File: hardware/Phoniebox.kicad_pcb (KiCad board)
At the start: 2 copper layers, 65 x 56.5 mm, 84 parts, among them J1 GPIO, J2 Screw_Terminal_01x08, J3 Screw_Terminal_01x08, J4 Screw_Terminal_01x08, J5 Conn_02x02_Odd_Even, J7 USB_C_Receptacle_USB2.0, J8 Conn_02x04_Odd_Even, Q1 2N7002, Q2 2N7002, Q3 2N7002, Q4 2N7002, Q5 2N7002, Q6 2N7002, Q7 AO3401A, Q8 2N7002, U1 PAM8406, U2 TPS79333-EP, U3 PCM5102, U4 CAT24C32

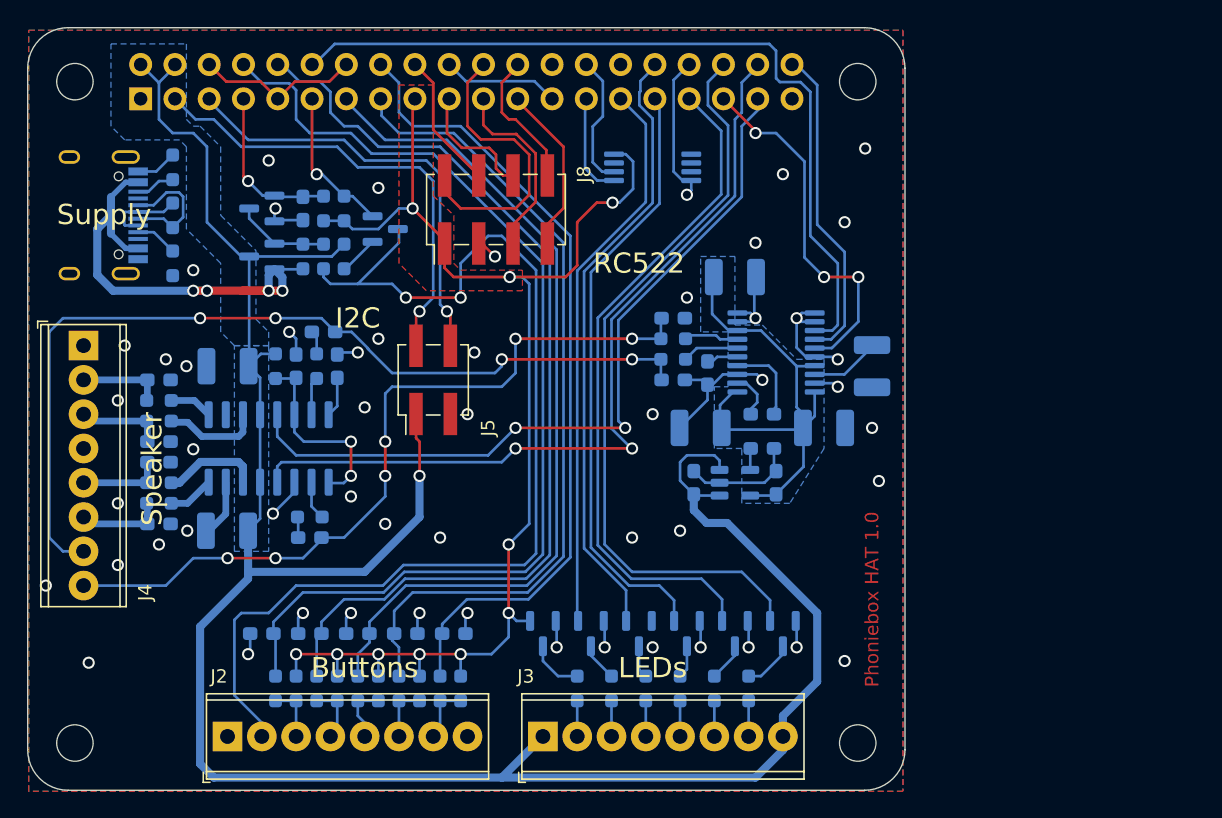
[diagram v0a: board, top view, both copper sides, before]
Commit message: Smaller high value caps. Standard R/C footprints instead of hand solder.
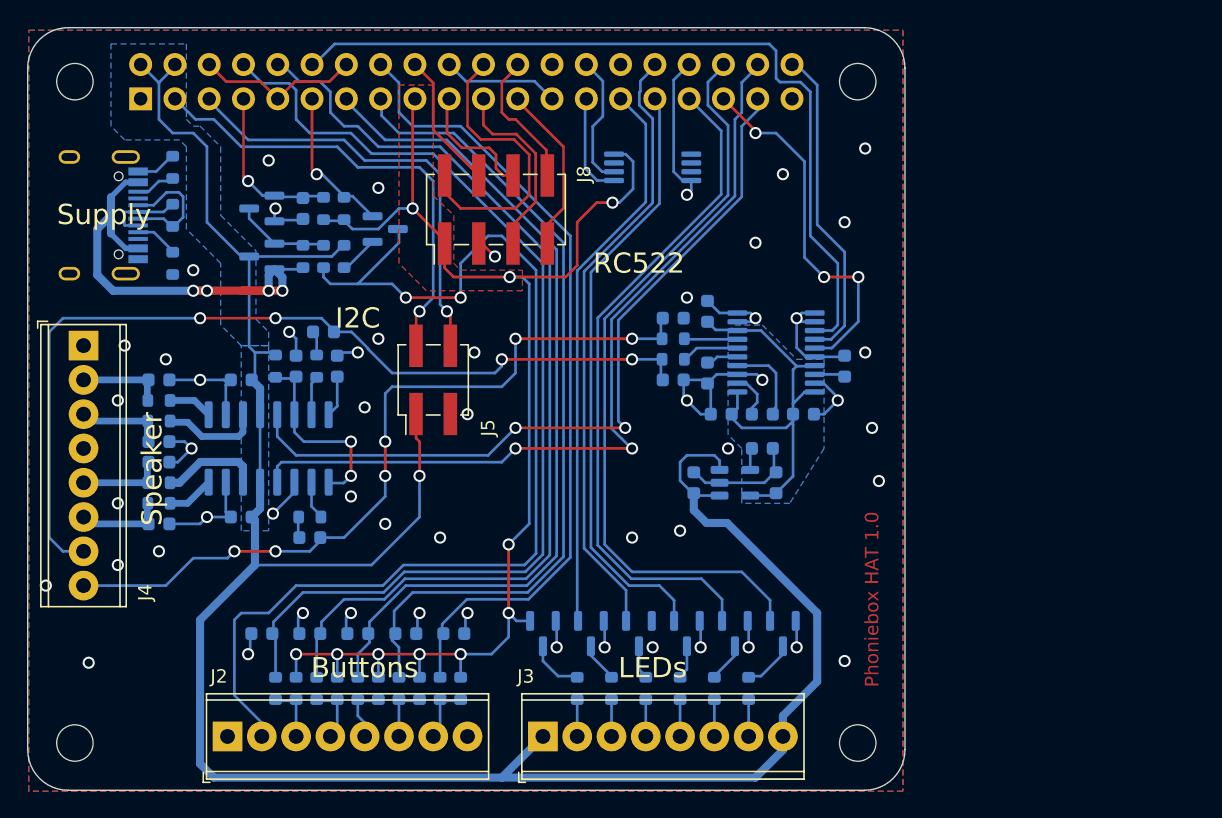
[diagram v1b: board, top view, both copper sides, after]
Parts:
- C10, C11, C12, C13, C14, C15, C16, C17, C2, C20, C21, C22, C24, C25, C27, C28, C3, C5, C6, C8, C9: footprint Capacitor_SMD:C_0603_1608Metric_Pad1.08x0.95mm_HandSolder -> Capacitor_SMD:C_0603_1608Metric
- C18, C19, C23, C26, C4, C7: footprint Capacitor_SMD:C_1210_3225Metric_Pad1.33x2.70mm_HandSolder -> Capacitor_SMD:C_0603_1608Metric
- FB1, FB2, FB3, FB4, R1, R10, R11, R12, R13, R14, R15, R16, R17, R18, R19, R2, R20, R21, R22, R23, R24, R25, R26, R27, R28, R3, R30, R4, R5, R6, R7, R8, R9: footprint Resistor_SMD:R_0603_1608Metric_Pad0.98x0.95mm_HandSolder -> Resistor_SMD:R_0603_1608Metric
- moved C19 3.25 mm to (150.4, 64.5), turned to 90 degrees
- moved C26 2.03 mm to (160.5, 68.6), turned to 90 degrees
- moved C23 1.83 mm to (157.5, 72.1)
- moved C18 1.83 mm to (151.4, 72.1)
- moved C7 1.46 mm to (115.8, 79.8)
- moved C4 1.44 mm to (115.8, 69.6)
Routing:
- net GND: track 104.2 -> 122.9 mm, vias 54 -> 55
- net +3.3VA: track 37.1 -> 30.5 mm
- net /Audio/LDOO: track 4.92 -> 2.29 mm
- net +5V: track 174.5 -> 173.4 mm

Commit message: Move a lot of parts. Switch audio l/r (only in schematic). Next step: Apply in PCB.
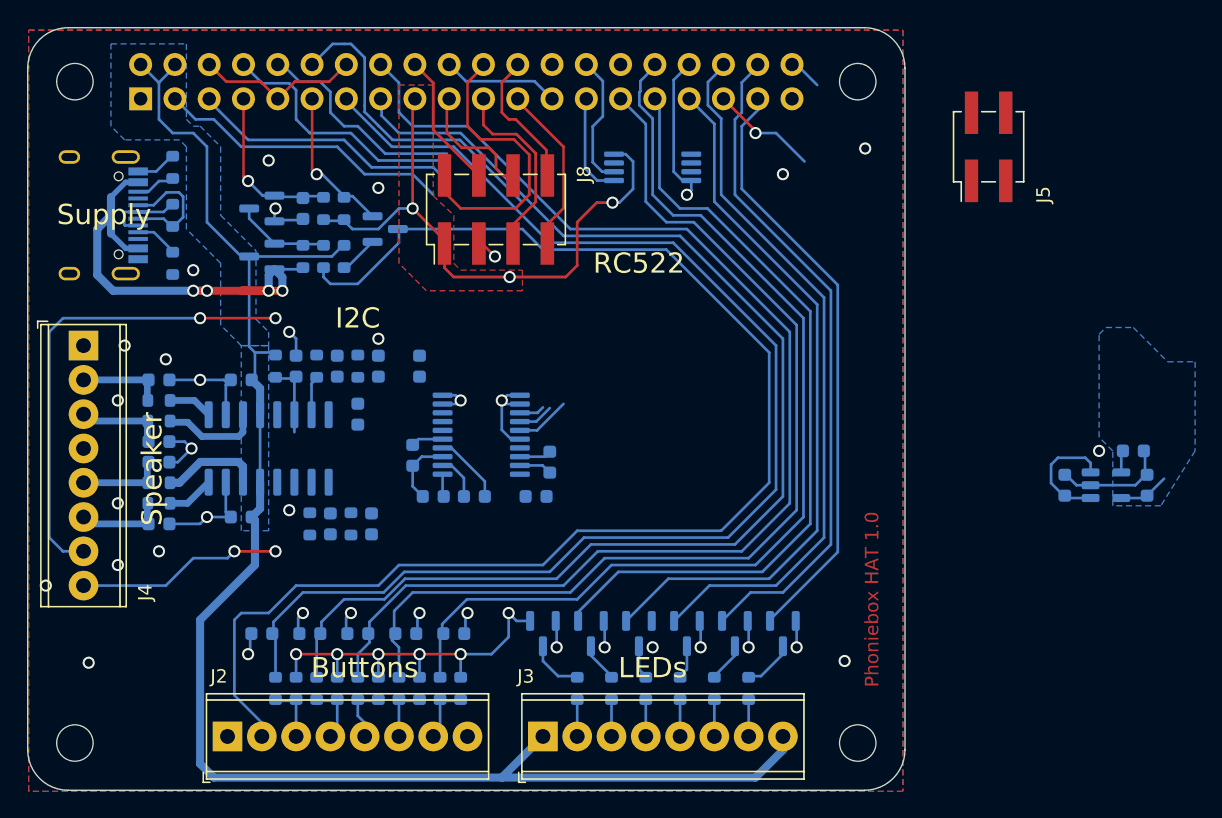
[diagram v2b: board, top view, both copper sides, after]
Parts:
- moved J5 44.6 mm to (171.2, 52.3)
- moved R23 27.5 mm to (124.0, 80.3), turned to -90 degrees
- moved C20 27.5 mm to (181.9, 74.9)
- moved C17 27.5 mm to (176.8, 77.4)
- moved C22 27.5 mm to (182.9, 77.4)
- moved U2 27.5 mm to (179.9, 77.4)
- moved C28 27.1 mm to (125.5, 80.3), turned to 90 degrees
- moved R22 23.4 mm to (124.5, 68.6), turned to -90 degrees
- moved C26 23.0 mm to (138.7, 75.7), turned to -90 degrees
- moved C25 22.7 mm to (128.5, 75.2)
- moved U3 22.7 mm to (133.6, 73.7)
- moved C18 22.2 mm to (130.0, 78.2)
- moved C24 22.2 mm to (133.1, 78.2)
- moved C27 21.9 mm to (126.0, 68.6), turned to -90 degrees
- moved C19 21.7 mm to (129.0, 68.6)
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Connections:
- C14 pad 1: /GPIO27 -> /GPIO23
- C15 pad 1: /GPIO22 -> /GPIO5
- C16 pad 1: /GPIO23 -> /GPIO12
- C8 pad 1: /GPIO14 -> /GPIO27
- C9 pad 1: /GPIO15 -> /GPIO22
- Q2 pad 1: /GPIO6 -> /GPIO16
- Q3 pad 1: /GPIO5 -> /GPIO6
- Q4 pad 1: /GPIO13 -> /GPIO20
- Q5 pad 1: /GPIO12 -> /GPIO13
- Q6 pad 1: /GPIO16 -> /GPIO26
- R11 pad 1: /GPIO27 -> /GPIO23
- R13 pad 1: /GPIO22 -> /GPIO5
- R21 pad 1: /GPIO23 -> /GPIO12
- R7 pad 1: /GPIO14 -> /GPIO27
- R9 pad 1: /GPIO15 -> /GPIO22
- U1 pad 12: /GPIO20 -> /GPIO15
- U1 pad 5: /GPIO26 -> /GPIO14
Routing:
- net /GPIO14: track 77.2 -> 18.8 mm
- net /GPIO15: track 72.2 -> 16.2 mm
- net +5V: track 173.4 -> 128.3 mm, vias 1 -> 0
- net /INR: track 57.9 -> 15.3 mm, vias 6 -> 2
- net /GPIO18: track 60.2 -> 25.3 mm
- net /GPIO5: track 41.5 -> 75.0 mm
- net /INL: track 67.9 -> 35.4 mm, vias 4 -> 2
- net /GPIO27: track 63.2 -> 95.5 mm
- net /GPIO23: track 59.8 -> 91.6 mm
- net /GPIO22: track 61.1 -> 91.6 mm
- net /GPIO12: track 45.5 -> 74.2 mm
- net +3V3: track 98.4 -> 71.7 mm, vias 10 -> 9
- net +3.3VA: track 30.5 -> 5.44 mm
- net /Button_1: track 81.6 -> 103.0 mm, vias 2 -> 0
- net /GPIO21: track 23.7 -> 5.02 mm
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
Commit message: Moved DAC. Replace pin headers with single row SMD ones (compatible with RC522/display PCBs to connect).
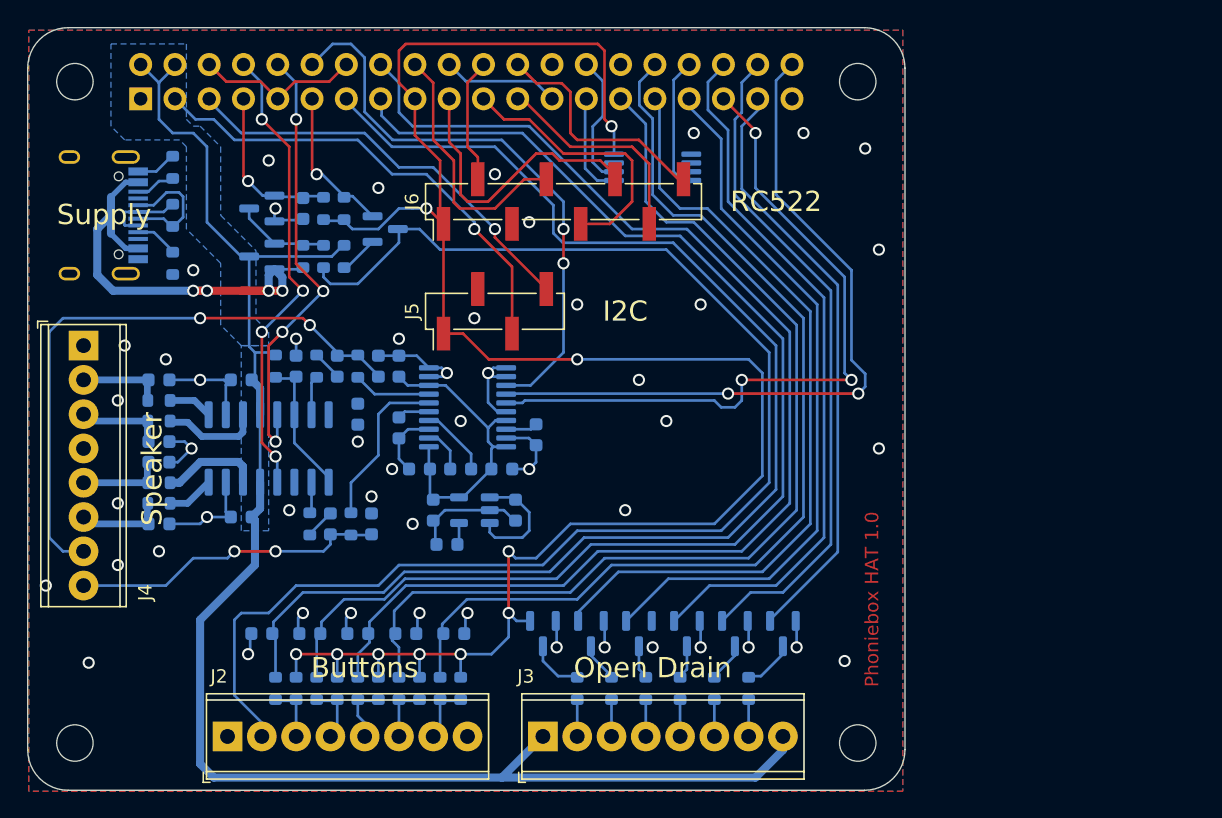
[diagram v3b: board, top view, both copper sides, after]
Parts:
- removed J8: Conn_02x04_Odd_Even, Connector_PinHeader_2.54mm:PinHeader_2x04_P2.54mm_Vertical_SMD
- added J6: Conn_01x08_Male, Connector_PinHeader_2.54mm:PinHeader_1x08_P2.54mm_Vertical_SMD_Pin1Left, F.Cu at (139.7, 56.4)
- J5: value Conn_02x02_Odd_Even -> Conn_01x04_Male; footprint Connector_PinHeader_2.54mm:PinHeader_2x02_P2.54mm_Vertical_SMD -> Connector_PinHeader_2.54mm:PinHeader_1x04_P2.54mm_Vertical_SMD_Pin1Left
- moved C22 52.9 mm to (130.0, 79.2), turned to 90 degrees
- moved C20 51.3 mm to (131.1, 81.8), turned to 0 degrees
- moved U2 46.8 mm to (133.1, 79.2), turned to 180 degrees
- moved C17 40.7 mm to (136.1, 79.2), turned to 90 degrees
- moved J5 38.6 mm to (134.6, 64.5)
- moved C23 3.25 mm to (135.1, 76.2)
- moved U3 2.27 mm to (132.6, 71.6)
- moved C25 2.27 mm to (127.5, 73.2)
- moved C18 2.27 mm to (129.0, 76.2)
- moved C24 2.27 mm to (132.1, 76.2)
- moved C26 2.27 mm to (137.7, 73.7)
- moved C19 1.52 mm to (127.5, 68.6)
- turned C2 to -90 degrees
- turned R22 to 90 degrees
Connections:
- C2 pad 1: /INL -> /INR
- C2 pad 2: /Audio/INL1 -> /Audio/INR1
- C27 pad 2: /INL -> /INR
- C28 pad 1: /INR -> /INL
- C3 pad 1: /INR -> /INL
- C3 pad 2: /Audio/INR1 -> /Audio/INL1
- FB1 pad 1: /Audio/LOUT+ -> /Audio/ROUT+
- FB2 pad 1: /Audio/LOUT- -> /Audio/ROUT-
- FB3 pad 1: /Audio/ROUT- -> /Audio/LOUT-
- FB4 pad 1: /Audio/ROUT+ -> /Audio/LOUT+
- J4 pad 7: /INL -> /INR
- J4 pad 8: /INR -> /INL
- J5 pad 1: +5V -> +3V3
- J5 pad 2: /GPIO2_SDA -> GND
- J5 pad 3: GND -> /GPIO2_SDA
- R22 pad 1: /Audio/OUTL -> /Audio/OUTR
- R22 pad 2: /INL -> /INR
- R23 pad 1: /Audio/OUTR -> /Audio/OUTL
- R23 pad 2: /INR -> /INL
- R3 pad 1: /Audio/INL1 -> /Audio/INR1
- R3 pad 2: /Audio/INL2 -> /Audio/INR2
- R4 pad 1: /Audio/INR1 -> /Audio/INL1
- R4 pad 2: /Audio/INR2 -> /Audio/INL2
- U1 pad 1: /Audio/LOUT+ -> /Audio/ROUT+
- U1 pad 10: /Audio/INR2 -> /Audio/INL2
- U1 pad 12: /GPIO15 -> /GPIO14
- U1 pad 14: /Audio/ROUT- -> /Audio/LOUT-
- U1 pad 16: /Audio/ROUT+ -> /Audio/LOUT+
- U1 pad 3: /Audio/LOUT- -> /Audio/ROUT-
- U1 pad 5: /GPIO14 -> /GPIO15
- U1 pad 7: /Audio/INL2 -> /Audio/INR2
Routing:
- net +3V3: track 71.7 -> 141.5 mm, vias 9 -> 10
- net /GPIO21: track 5.02 -> 53.9 mm, vias 0 -> 2
- net /GPIO19: track 12.0 -> 52.3 mm, vias 1 -> 3
- net /INR: track 15.3 -> 45.0 mm
- net +3.3VA: track 5.44 -> 23.3 mm
- net /GPIO18: track 25.3 -> 42.9 mm, vias 0 -> 2
- net /GPIO15: track 16.2 -> 33.3 mm, vias 0 -> 4
- net /GPIO14: track 18.8 -> 34.5 mm, vias 0 -> 4
- net /GPIO2_SDA: track 22.0 -> 35.3 mm, vias 0 -> 1
- net /RST: track 22.0 -> 9.26 mm
- net /Audio/OUTL: track 0.00 -> 12.2 mm
- net /MOSI: track 9.36 -> 21.5 mm
- net /INL: track 35.4 -> 23.4 mm
- net /GPIO3_SCL: track 19.4 -> 31.2 mm, vias 0 -> 1
- net /IRQ: track 10.1 -> 19.4 mm
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- removed copper zone on B.Cu, net +3.3VA
- removed copper zone on F.Cu, net +3V3
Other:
- board text added: "Open Drain"
- board text removed: "LEDs"

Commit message: Size 0805 for 10uF capacitors.
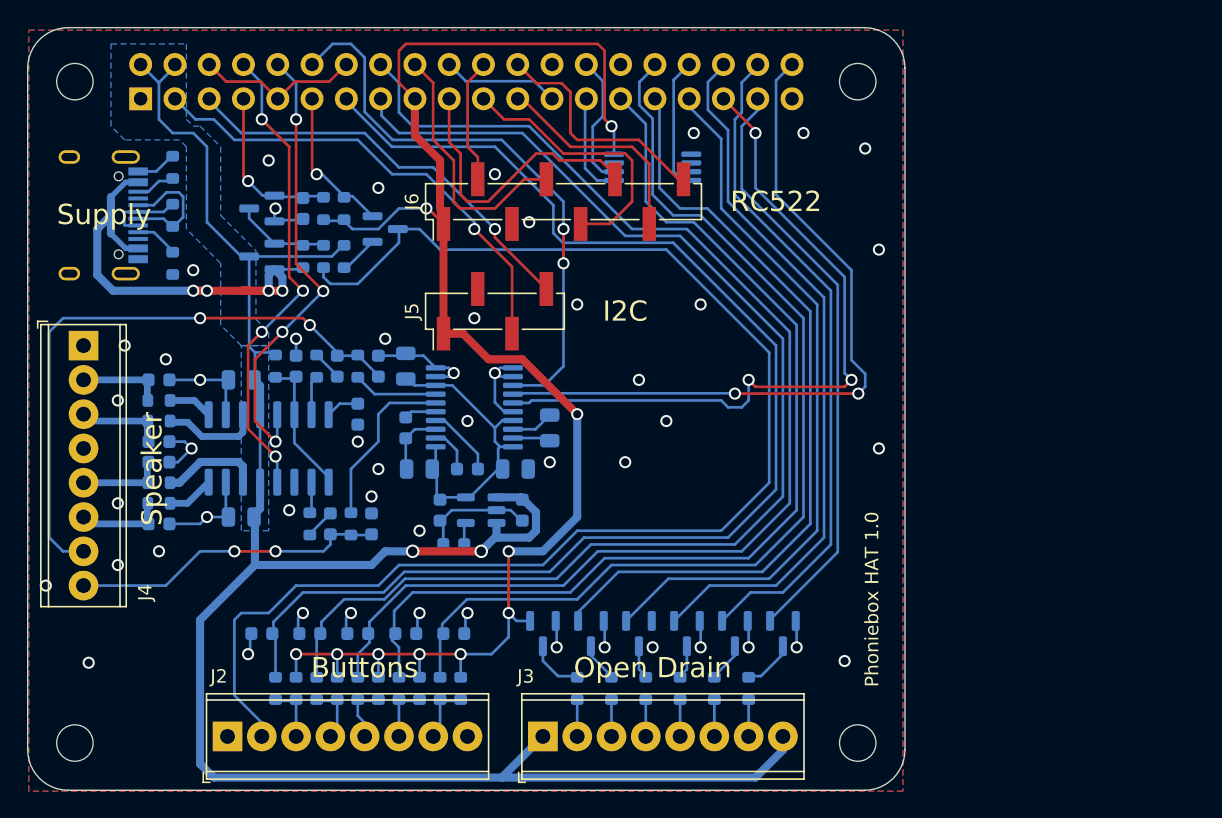
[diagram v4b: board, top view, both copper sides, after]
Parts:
- C18, C19, C23, C26, C4, C7: footprint Capacitor_SMD:C_0603_1608Metric -> Capacitor_SMD:C_0805_2012Metric
- moved C26 1.13 mm to (138.7, 73.2)
- moved C23 1.01 mm to (136.1, 76.2)
- moved C19 0.51 mm to (128.0, 68.6)
- moved C25 0.50 mm to (128.0, 73.2)
- moved C17 0.50 mm to (136.6, 79.2)
- moved C20 0.50 mm to (131.6, 81.8)
- moved C22 0.50 mm to (130.6, 79.2)
- moved C24 0.50 mm to (132.6, 76.2)
- moved U2 0.50 mm to (133.6, 79.2)
- moved U3 0.50 mm to (133.1, 71.6)
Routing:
- net +3V3: track 141.5 -> 113.7 mm
- net +5V: track 128.3 -> 147.4 mm, vias 0 -> 2
- net GND: track 108.4 -> 105.6 mm
- net Net-(C6-Pad1): track 0.00 -> 2.50 mm
- net /GPIO14: track 34.5 -> 35.3 mm
- net /GPIO15: track 33.3 -> 34.1 mm
- net /Audio/LDOO: track 2.37 -> 3.16 mm
